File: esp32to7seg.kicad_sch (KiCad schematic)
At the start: 31 parts, among them J1 Conn_01x05, J2 Barrel_Jack_Switch, J3 Conn_01x03, Q17 BC848, Q18 BC848, SW1 SW_Push, U1 LT1117-3.3, U2 ESP32-C3-WROOM-02

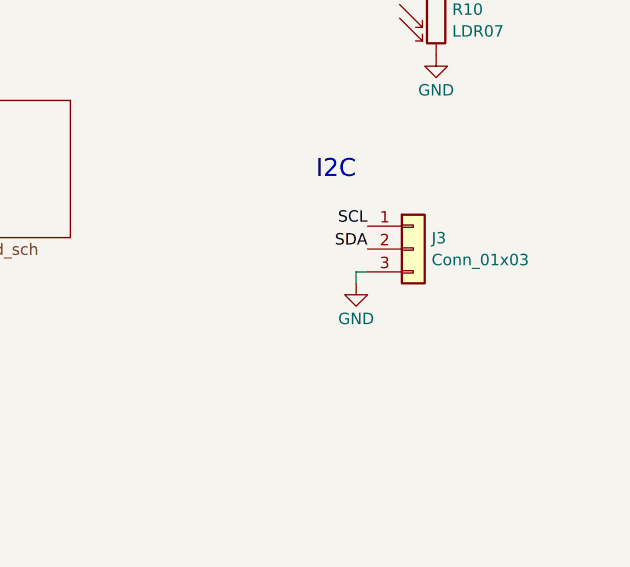
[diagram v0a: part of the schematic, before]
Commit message: Add 3v3 pin to i2c header.
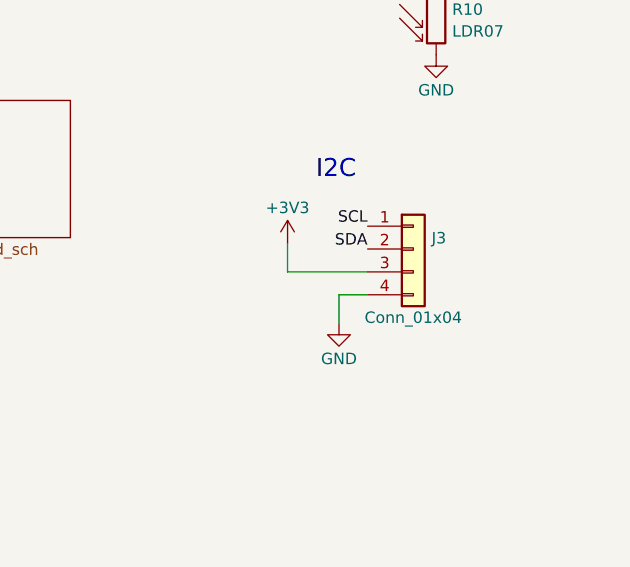
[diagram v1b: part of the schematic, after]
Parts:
- J3: value Conn_01x03 -> Conn_01x04; footprint Connector_PinHeader_2.54mm:PinHeader_1x03_P2.54mm_Vertical -> Connector_PinHeader_2.54mm:PinHeader_1x04_P2.54mm_Vertical; symbol Connector_Generic:Conn_01x03 -> Connector_Generic:Conn_01x04
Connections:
- net +3V3: now also J3.3 (Pin_3)
- net GND: now also J3.4 (Pin_4); no longer J3.3 (Pin_3)
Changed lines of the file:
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@@
   (no_connect (at 114.3 54.61))
   (no_connect (at 114.3 43.18))
-  (wire (pts (xy 255.27 72.39) (xy 254 72.39))
+  (wire (pts (xy 255.27 74.93) (xy 252.095 74.93))
     (stroke (width 0) (type default))
   )
@@
     (stroke (width 0) (type default))
   )
+  (wire (pts (xy 252.095 74.93) (xy 252.095 78.105))
+    (stroke (width 0) (type default))
+  )
   (wire (pts (xy 144.78 39.37) (xy 165.735 39.37))
     (stroke (width 0) (type default))
@@
     (stroke (width 0) (type default))
   )
-  (wire (pts (xy 254 72.39) (xy 254 73.66))
-    (stroke (width 0) (type default))
-  )
   (wire (pts (xy 44.45 160.02) (xy 44.45 157.48))
     (stroke (width 0) (type default))
   )
+  (wire (pts (xy 255.27 72.39) (xy 246.38 72.39))
+    (stroke (width 0) (type default))
+  )
   (wire (pts (xy 110.49 24.13) (xy 110.49 25.4))
     (stroke (width 0) (type default))
@@
   )
   (wire (pts (xy 34.29 109.22) (xy 34.29 113.03))
+    (stroke (width 0) (type default))
+  )
+  (wire (pts (xy 246.38 69.215) (xy 246.38 72.39))
     (stroke (width 0) (type default))
   )
@@
     (effects (font (size 1.27 1.27)) (justify right bottom))
   )
-  (symbol (lib_id "Connector_Generic:Conn_01x03") (at 260.35 69.85 0) (unit 1)
+  (symbol (lib_id "Connector_Generic:Conn_01x04") (at 260.35 69.85 0) (unit 1)
     (in_bom yes) (on_board yes) (dnp no) (fields_autoplaced)
     (property "Reference" "J3" (at 262.382 68.6379 0)
       (effects (font (size 1.27 1.27)) (justify left))
     )
-    (property "Value" "Conn_01x03" (at 262.382 71.0621 0)
-      (effects (font (size 1.27 1.27)) (justify left))
-    )
-    (property "Footprint" "Connector_PinHeader_2.54mm:PinHeader_1x03_P2.54mm_Vertical" (at 260.35 69.85 0)
+    (property "Value" "Conn_01x04" (at 260.35 77.47 0)
+      (effects (font (size 1.27 1.27)))
+    )
+    (property "Footprint" "Connector_PinHeader_2.54mm:PinHeader_1x04_P2.54mm_Vertical" (at 260.35 69.85 0)
       (effects (font (size 1.27 1.27)) hide)
     )
@@
     (pin "2")
     (pin "3")
+    (pin "4")
     (instances
       (project "esp32to7seg"
@@
     )
   )
+  (symbol (lib_id "power:+3V3") (at 246.38 69.215 0) (unit 1)
+    (in_bom yes) (on_board yes) (dnp no) (fields_autoplaced)
+    (property "Reference" "#PWR044" (at 246.38 73.025 0)
+      (effects (font (size 1.27 1.27)) hide)
+    )
+    (property "Value" "+3V3" (at 246.38 65.27 0)
+      (effects (font (size 1.27 1.27)))
+    )
+    (property "Footprint" "" (at 246.38 69.215 0)
+      (effects (font (size 1.27 1.27)) hide)
+    )
+    (property "Datasheet" "" (at 246.38 69.215 0)
+      (effects (font (size 1.27 1.27)) hide)
+    )
+    (pin "1")
+    (instances
+      (project "kitchenclock"
+        (path "/99eef389-f87f-4102-902d-02c6c6086bba"
+          (reference "#PWR044") (unit 1)
+        )
+      )
+      (project "esp32to7seg"
+        (path "/9c1fcffb-d276-4c8d-bbc2-82ffcadbaa7b"
+          (reference "#PWR047") (unit 1)
+        )
+      )
+    )
+  )
   (symbol (lib_id "power:GND") (at 44.45 162.56 0) (unit 1)
     (in_bom yes) (on_board yes) (dnp no) (fields_autoplaced)
@@
     )
   )
-  (symbol (lib_id "power:GND") (at 254 73.66 0) (unit 1)
-    (in_bom yes) (on_board yes) (dnp no) (fields_autoplaced)
-    (property "Reference" "#PWR017" (at 254 80.01 0)
-      (effects (font (size 1.27 1.27)) hide)
-    )
-    (property "Value" "GND" (at 254 77.605 0)
-      (effects (font (size 1.27 1.27)))
-    )
-    (property "Footprint" "" (at 254 73.66 0)
-      (effects (font (size 1.27 1.27)) hide)
-    )
-    (property "Datasheet" "" (at 254 73.66 0)
-      (effects (font (size 1.27 1.27)) hide)
-    )
+  (symbol (lib_id "power:GND") (at 252.095 78.105 0) (unit 1)
+    (in_bom yes) (on_board yes) (dnp no) (fields_autoplaced)
+    (property "Reference" "#PWR017" (at 252.095 84.455 0)
+      (effects (font (size 1.27 1.27)) hide)
+    )
+    (property "Value" "GND" (at 252.095 82.05 0)
+      (effects (font (size 1.27 1.27)))
+    )
+    (property "Footprint" "" (at 252.095 78.105 0)
+      (effects (font (size 1.27 1.27)) hide)
+    )
+    (property "Datasheet" "" (at 252.095 78.105 0)
+      (effects (font (size 1.27 1.27)) hide)
+    )

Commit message: Multiple improvements
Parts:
- removed J1: Conn_01x05, Connector_PinHeader_2.54mm:PinHeader_1x05_P2.54mm_Vertical, symbol Connector_Generic:Conn_01x05
- removed Q17, Q18: BC848, Package_TO_SOT_SMD:SOT-23, symbol Transistor_BJT:BC848
- removed R40, R9: 10k, Resistor_SMD:R_0805_2012Metric, symbol Device:R
- added J1: Conn_01x04_Pin, Connector_PinHeader_2.54mm:PinHeader_1x04_P2.54mm_Vertical, symbol Connector:Conn_01x04_Pin
- added R44: 10k, Resistor_SMD:R_0805_2012Metric, symbol Device:R
- added SW2: SW_Push, Button_Switch_THT:SW_PUSH_6mm, symbol Switch:SW_Push
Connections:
- net +3V3: now also R44.1
- net GND: now also J1.4 (Pin_4), SW2.1
- net Led Driver/CLK: now also U2.5 (IO6); no longer U2.13 (IO18)
- net Led Driver/DIN: now also U2.6 (IO7); no longer U2.10 (IO10)
- net Led Driver/~{CS}: now also U2.4 (IO5); no longer U2.14 (IO19)
- net RXD: no longer names the net of U2.11 (RXD)
- net TXD: no longer names the net of U2.12 (TXD)
- new net BUTTON2: R44.2, SW2.2, U2.10 (IO10)
- new net USB+: J1.2 (Pin_2), U2.14 (IO19)
- new net USB-: J1.3 (Pin_3), U2.13 (IO18)
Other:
- note removed: "Boot Mode: Pin | SPI | Download ------------------ IO2 | high | high IO8 | don't care | high IO9 | high | low"
- moved on the sheet: C5, R2, R41, SW1
